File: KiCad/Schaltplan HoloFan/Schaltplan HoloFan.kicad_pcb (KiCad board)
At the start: 2 copper layers, 19 parts, among them Q1 2N3904, Q2 2N3904, U1 NUCLEO-L432KC

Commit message: Python Programm Update + Timer Interrupt
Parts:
- added 12V_GND1: Conn_01x01_Pin, Connector_PinHeader_1.00mm:PinHeader_1x01_P1.00mm_Vertical, F.Cu at (288.1, 84.8)
- added 12V_GND2: MountingHole_Pad, MountingHole:MountingHole_2.2mm_M2, F.Cu at (288.1, 84.8)
- added Q3: 2N3904, Package_TO_SOT_THT:TO-92_Inline, F.Cu at (341.7, 124.0)
- added Q4: 2N3904, Package_TO_SOT_THT:TO-92_Inline, F.Cu at (341.6, 128.9)
- added R5: 2.2k, Resistor_THT:R_Axial_DIN0207_L6.3mm_D2.5mm_P7.62mm_Horizontal, F.Cu at (351.8, 126.7)
- added R6: 6.8k, Resistor_THT:R_Axial_DIN0207_L6.3mm_D2.5mm_P7.62mm_Horizontal, F.Cu at (328.6, 126.6)
- added R7: 2.2k, Resistor_THT:R_Axial_DIN0207_L6.3mm_D2.5mm_P7.62mm_Horizontal, F.Cu at (351.8, 130.4)
- added R8: 6.8k, Resistor_THT:R_Axial_DIN0207_L6.3mm_D2.5mm_P7.62mm_Horizontal, F.Cu at (328.5, 129.8)
- moved R1 221.8 mm to (351.8, 138.8), turned to 180 degrees
- moved U1 218.7 mm to (329.9, 151.3), turned to 90 degrees
- moved R3 217.9 mm to (351.9, 134.0), turned to 180 degrees
- moved Q1 200.9 mm to (341.5, 138.6), turned to 180 degrees
- moved Q2 196.7 mm to (341.6, 133.7), turned to 180 degrees
- moved 3V3_GND1 191.3 mm to (316.4, 128.0)
- moved 3V3_GND2 191.3 mm to (316.4, 128.0)
- moved 3V3_OUT1 179.3 mm to (316.6, 117.3)
- moved 3V3_OUT2 179.3 mm to (316.6, 117.3)
- moved R2 174.2 mm to (328.6, 138.6), turned to 0 degrees
- moved R4 168.9 mm to (328.6, 133.7), turned to 0 degrees
- moved 5V_GND1 161.4 mm to (309.6, 84.8)
- moved 5V_GND2 161.4 mm to (309.6, 84.8)
- moved 5V_IN1 145.4 mm to (292.8, 116.7)
- moved 5V_IN2 145.4 mm to (292.8, 116.7)
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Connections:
- U1 pad A3: DI_IN -> unconnected-(U1B-PA4-PadA3)
- U1 pad A5: unconnected-(U1B-PA6-PadA5) -> DI_IN
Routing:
- net CLK_IN: track 43.1 -> 27.5 mm
- net DI_IN: track 25.6 -> 39.0 mm
- net Net-(Q3-B): track 0.00 -> 5.60 mm
- net Net-(Q4-B): track 0.00 -> 5.60 mm
- net 3V3: track 24.0 -> 19.3 mm
- net DI_OUT2: track 0.00 -> 4.17 mm
- net 5V: track 8.69 -> 12.1 mm
- net CLK_OUT2: track 0.00 -> 3.37 mm
- net CLK_OUT: track 6.15 -> 2.91 mm
- net DI_OUT: track 5.98 -> 2.74 mm
- net Net-(Q2-B): track 7.62 -> 6.07 mm
- net Net-(Q1-B): track 7.58 -> 6.46 mm

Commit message: Finishing of HoloFan Project
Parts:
- removed 12V_GND2, 12V_IN1, 3V3_GND1, 3V3_OUT1, 5V_GND1, 5V_IN1, 5V_OUT1: MountingHole_Pad, MountingHole:MountingHole_2.2mm_M2
- removed Q3, Q4: 2N3904, Package_TO_SOT_THT:TO-92_Inline
- removed R5, R7: 2.2k, Resistor_THT:R_Axial_DIN0207_L6.3mm_D2.5mm_P7.62mm_Horizontal
- removed R6, R8: 6.8k, Resistor_THT:R_Axial_DIN0207_L6.3mm_D2.5mm_P7.62mm_Horizontal
- added 5V_GND3: Conn_01x01_Pin, Connector_PinHeader_1.00mm:PinHeader_1x01_P1.00mm_Vertical, F.Cu at (285.6, 127.0)
- added LED_1: Conn_01x04_Pin, APA102:APA102_Pads, F.Cu at (319.1, 96.7)
- added LED_2: Conn_01x04_Pin, APA102:APA102_Pads, F.Cu at (340.9, 96.7)
- added REF**: MountingHole_2.2mm_M2, MountingHole:MountingHole_2.2mm_M2, F.Cu at (330.0, 101.2)
- Q1, Q2: footprint Package_TO_SOT_THT:TO-92_Inline -> Package_TO_SOT_SMD:TSOT-23
- R1, R2, R3, R4: footprint Resistor_THT:R_Axial_DIN0207_L6.3mm_D2.5mm_P7.62mm_Horizontal -> Resistor_SMD:R_0603_1608Metric
- moved R4 32.5 mm to (353.4, 112.7), turned to -90 degrees
- moved R2 32.0 mm to (347.4, 112.8), turned to -90 degrees
- moved U1 22.9 mm to (343.2, 132.6)
- moved Q1 22.7 mm to (347.5, 116.7), turned to 90 degrees
- moved Q2 20.6 mm to (353.4, 116.8), turned to 90 degrees
- moved R1 18.4 mm to (347.9, 120.9), turned to 90 degrees
- moved R3 13.3 mm to (353.8, 120.9), turned to 90 degrees
- moved 3V3_OUT2 7.60 mm to (309.1, 116.1)
- moved 5V_IN2 7.60 mm to (285.2, 115.4)
- moved 3V3_GND2 7.34 mm to (309.1, 127.2)
- moved 12V_GND1 5.04 mm to (287.8, 89.9)
- moved 5V_GND2 5.04 mm to (309.3, 89.9)
- moved 5V_OUT2 5.04 mm to (309.3, 79.3)
- moved 12V_IN2 5.04 mm to (287.6, 79.2)
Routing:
- net GND: track 17.3 -> 195.9 mm
- net 5V: track 12.1 -> 169.7 mm, vias 0 -> 1
- net CLK_OUT: track 2.91 -> 49.9 mm, vias 0 -> 1
- net 3V3: track 19.3 -> 62.3 mm, vias 0 -> 1
- net DI_OUT: track 2.74 -> 43.9 mm, vias 0 -> 1
- net DI_IN: track 39.0 -> 12.0 mm
- net CLK_IN: track 27.5 -> 6.90 mm
- net Net-(Q3-B): track 5.60 -> 0.00 mm
- net Net-(Q4-B): track 5.60 -> 0.00 mm
- net Net-(Q1-B): track 6.46 -> 2.18 mm
- net DI_OUT2: track 4.17 -> 0.00 mm
- net Net-(Q2-B): track 6.07 -> 2.19 mm
- net CLK_OUT2: track 3.37 -> 0.00 mm
- added copper zone on B.Cu, net GND
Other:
- board outline added: 110 x 110 mm

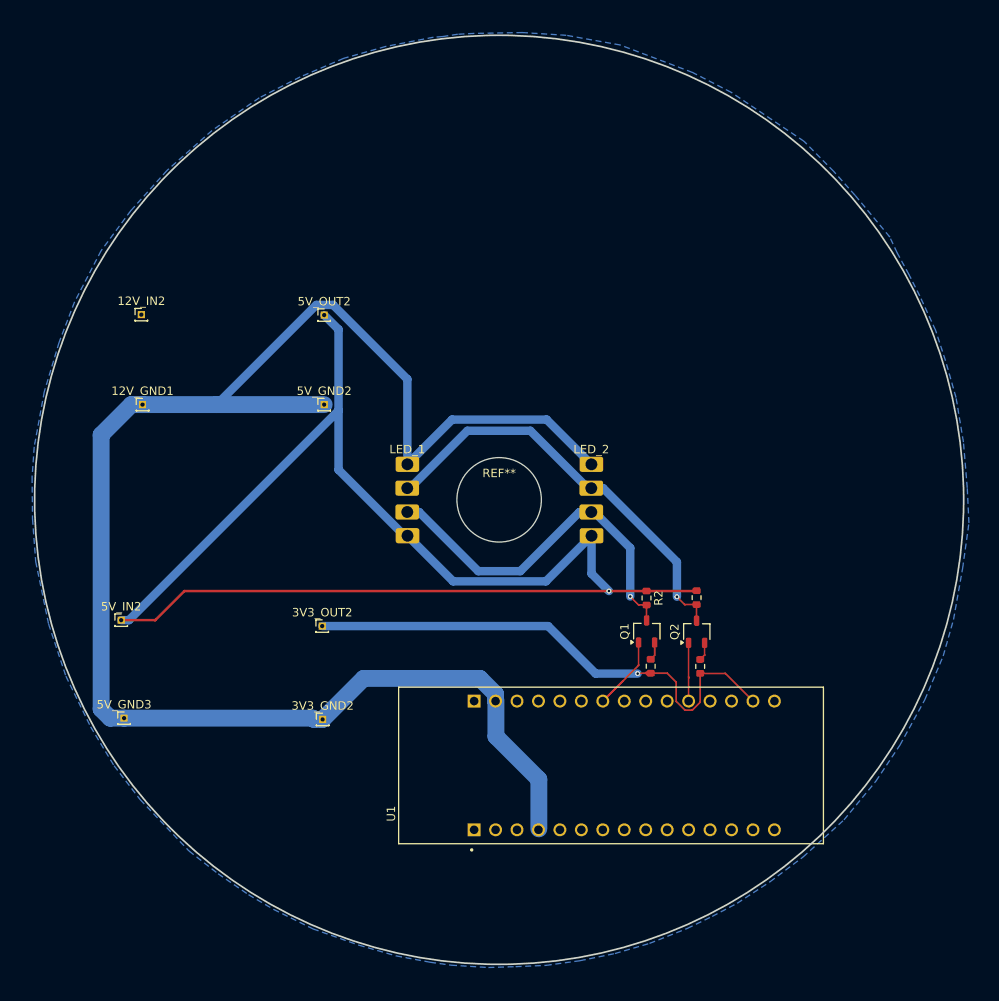
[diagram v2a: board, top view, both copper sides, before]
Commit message: PCB Layout Finishing
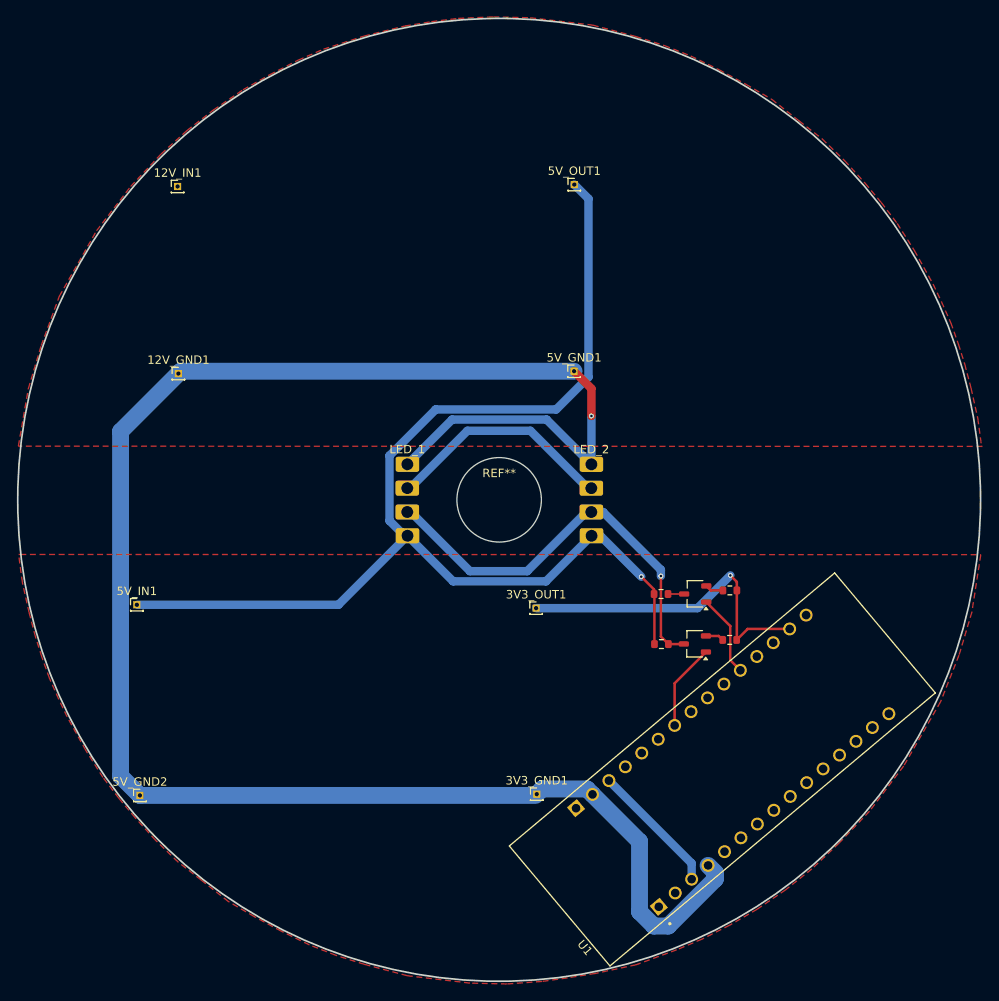
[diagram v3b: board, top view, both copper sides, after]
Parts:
- moved 5V_OUT1 33.4 mm to (338.9, 63.8)
- moved 5V_GND1 29.9 mm to (338.9, 85.9)
- moved 3V3_GND1 26.9 mm to (334.4, 136.0)
- moved 3V3_OUT1 25.4 mm to (334.4, 114.0)
- moved 12V_IN1 15.8 mm to (291.9, 64.0)
- moved U1 13.2 mm to (356.4, 133.1), turned to 130 degrees
- moved R1 9.86 mm to (357.3, 117.7), turned to 180 degrees
- moved R3 9.66 mm to (357.3, 111.9), turned to 180 degrees
- moved 5V_GND2 9.34 mm to (287.5, 136.2)
- moved Q1 5.90 mm to (353.2, 118.2), turned to 180 degrees
- moved R2 5.74 mm to (349.2, 118.2), turned to 0 degrees
- moved 12V_GND1 5.62 mm to (292.0, 86.2)
- moved Q2 4.48 mm to (353.2, 112.3), turned to 180 degrees
- moved R4 4.23 mm to (349.2, 112.3), turned to 0 degrees
- moved 5V_IN1 2.60 mm to (287.1, 113.6)
- renumbered 12V_IN2 to 12V_IN1, 3V3_GND2 to 3V3_GND1, 3V3_OUT2 to 3V3_OUT1, 5V_GND2 to 5V_GND1, 5V_GND3 to 5V_GND2, 5V_IN2 to 5V_IN1, 5V_OUT2 to 5V_OUT1
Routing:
- net 5V: track 169.7 -> 139.6 mm
- net GND: track 195.9 -> 222.9 mm, vias 0 -> 1
- net 3V3: track 62.3 -> 39.7 mm
- net CLK_OUT: track 49.9 -> 29.3 mm, vias 1 -> 0
- net unconnected-(U1A-NRST_CN3-PadRST): track 0.00 -> 15.7 mm
- net DI_OUT: track 43.9 -> 49.7 mm
- net CLK_IN: track 6.90 -> 9.76 mm
- net DI_IN: track 12.0 -> 10.2 mm
- added copper zone on F.Cu, net GND
- removed copper zone on B.Cu, net GND
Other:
- board size 110 x 110 mm -> 114 x 114 mm
